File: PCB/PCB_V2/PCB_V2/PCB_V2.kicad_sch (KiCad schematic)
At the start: 99 parts, among them J1 GND, J2 VIN, J3 GND, J4 VIN, J5 VOUT, J6 GND, J7 VOUT, J8 GND, Q1 BC817-40(SOT23), Q2 BC817-40(SOT23), T1 LMUN2211LT1G(SOT-23), U1 ESP32-WROOM-32E-N4, U2 CH340X(MSOP-10), U3 LAN8710A-EZC(QFN32)

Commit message: Changes Part 1 for the PCB Files
Most recent update for the PCB Design
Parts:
- removed C23, C24, C25, C26: C, symbol Device:C
- removed D5, D6: D, symbol Device:D
- removed J1, J3, J6, J8: GND, symbol Connector:Conn_01x01_Pin
- removed J2, J4: VIN, symbol Connector:Conn_01x01_Pin
- removed J5, J7: VOUT, symbol Connector:Conn_01x01_Pin
- removed L3, L4: L, symbol Device:L
- removed R24, R25, R26, R27, R28, R29, R30, R31: R_US, symbol Device:R_US
- removed R34: 52.3k, symbol Jumper:SolderJumper_2_Open
- removed R35, R37: 10k, symbol Device:R_US
- removed R36: 140k, symbol Jumper:SolderJumper_2_Open
- removed U4, U5: ~, symbol buck converter module:mp1584
- added D10, D8, D9: 1N4007, Diode_THT:D_DO-41_SOD81_P10.16mm_Horizontal, symbol Diode:1N4007
- added D11: 1N5822, Diode_THT:D_DO-201AD_P15.24mm_Horizontal, symbol Diode:1N5822
- added D5, D6, D7: LED, LED_THT:LED_D3.0mm, symbol Device:LED
- added J11, J12, J13: Screw_Terminal_01x03, TerminalBlock_Phoenix:TerminalBlock_Phoenix_MKDS-1,5-3-5.08_1x03_P5.08mm_Horizontal, symbol Connector:Screw_Terminal_01x03
- added J14: PSU_I/P, TerminalBlock_Phoenix:TerminalBlock_Phoenix_MKDS-1,5-3-5.08_1x03_P5.08mm_Horizontal, symbol Connector:Screw_Terminal_01x02
- added J15: Battery_I/P, TerminalBlock_Phoenix:TerminalBlock_Phoenix_MKDS-1,5-3-5.08_1x03_P5.08mm_Horizontal, symbol Connector:Screw_Terminal_01x02
- added J19: LEDs Ground, symbol Connector:Screw_Terminal_01x03
- added K1, K2, K3: FINDER-34.51.7xxx.x019, Relay_THT:Relay_SPDT_Finder_34.51_Horizontal, symbol Relay:FINDER-34.51.7xxx.x019
- added Q3, Q4, Q5: BC546, Package_TO_SOT_THT:TO-92_Inline, symbol Transistor_BJT:BC546
- added R24, R26: 140k, Resistor_SMD:R_0603_1608Metric_Pad0.98x0.95mm_HandSolder, symbol Device:R
- added R25, R27, R29: 10k, Resistor_SMD:R_0603_1608Metric_Pad0.98x0.95mm_HandSolder, symbol Device:R
- added R28: 52.3k, Resistor_SMD:R_0603_1608Metric_Pad0.98x0.95mm_HandSolder, symbol Device:R
- added R30, R38, R40: 2.2k, Resistor_SMD:R_0805_2012Metric, symbol Device:R
- added R31, R39, R41: 3.3k, Resistor_SMD:R_0805_2012Metric, symbol Device:R
- added R32, R33, R34: 300, Resistor_SMD:R_0603_1608Metric, symbol Device:R
- added R35, R36, R37: 1k, Resistor_SMD:R_0603_1608Metric, symbol Device:R
- added R42, R44: 10k, symbol Device:R
- added R43, R45: 2.2k, symbol Device:R
- added U4: AMS1117-3.3, Package_TO_SOT_SMD:SOT-223-3_TabPin2, symbol Regulator_Linear:AMS1117-3.3
- added U5, U6, U7: ACS712xLCTR-20A, Package_SO:SOIC-8_3.9x4.9mm_P1.27mm, symbol Sensor_Current:ACS712xLCTR-20A
- C15: value C -> 10uF; footprint (none) -> Capacitor_SMD:C_0805_2012Metric
- C16, C19, C21: value C -> 100nF; footprint (none) -> Capacitor_SMD:C_0805_2012Metric
- C17, C20, C22: value C -> 1nF; footprint (none) -> Capacitor_SMD:C_0805_2012Metric
- C18: value C -> 22uF; footprint (none) -> Capacitor_SMD:C_0805_2012Metric
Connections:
- net GND: now also C15.2, C16.2, C17.2, C18.2, C19.2, C20.2, C21.2, C22.2, J14.2 (Pin_2), J15.2 (Pin_2), J19.1 (Pin_1), J19.2 (Pin_2), J19.3 (Pin_3), Q3.3 (E), Q4.3 (E), Q5.3 (E), R25.2, R27.2, R29.2, R31.2, R39.2, R41.2, R43.2, R45.2, U4.1 (GND), U5.5 (GND), U6.5 (GND), U7.5 (GND)
- net BC1_5_O/P: now reaches C19.1
- net BC1_5_O/P: now also C15.1, C16.1, C21.1, D10.1 (K), D8.1 (K), D9.1 (K), K1.A1, K2.A1, K3.A1, R28.1, R32.1, R33.1, R34.1, U4.3 (VI), U5.8 (VCC), U6.8 (VCC), U7.8 (VCC)
- net AMS1117_O/P: now reaches C18.1
- net AMS1117_O/P: now also U4.2 (VO); no longer C16.1
- net at C20.1: now also U6.6 (FILTER)
- net at C17.1: now also U5.6 (FILTER); no longer C15.1
- net at C22.1: now also U7.6 (FILTER)
- new net: R42.2, R43.1
- new net: R38.1, U6.7 (VIOUT)
- new net: D6.1 (K), D9.2 (A), K2.A2, Q4.1 (C)
- new net: Q4.2 (B), R36.1
- new net: U5.1 (IP+), U5.2 (IP+)
- new net: U5.3 (IP-), U5.4 (IP-)
- new net: R30.1, U5.7 (VIOUT)
- new net: D10.2 (A), D7.1 (K), K3.A2, Q5.1 (C)
- new net: D7.2 (A), R34.2
- new net: Q3.2 (B), R35.1
- new net: D5.1 (K), D8.2 (A), K1.A2, Q3.1 (C)
- new net: R28.2, R29.1
- new net: Q5.2 (B), R37.1
- new net: R40.1, U7.7 (VIOUT)
- new net: D5.2 (A), R32.2
- new net: R44.2, R45.1
- new net: D6.2 (A), R33.2
- new net +14.5V: D11.2 (A), J14.1 (Pin_1), R42.1
- new net BC2_12_O/P_1: R24.1
- new net BC3_12_O/P_2: R26.1, U6.1 (IP+), U6.2 (IP+), U7.1 (IP+), U7.2 (IP+)
- new net COM1: J11.2 (Pin_2), K1.11
- new net COM2: J12.2 (Pin_2), K2.11, U6.3 (IP-), U6.4 (IP-)
- new net COM3: J13.2 (Pin_2), K3.11, U7.3 (IP-), U7.4 (IP-)
- new net CURRENT_SENSE_1: R30.2, R31.1
- new net CURRENT_SENSE_2: R38.2, R39.1
- new net CURRENT_SENSE_3: R40.2, R41.1
- new net MAIN_OP: D11.1 (K), J15.1 (Pin_1), R44.1
- new net MP1584ENCircuit1/Feedback: R24.2, R25.1
- new net MP1584ENCircuit2/Feedback: R26.2, R27.1
- new net NC1: J11.1 (Pin_1), K1.12
- new net NC2: J12.1 (Pin_1), K2.12
- new net NC3: J13.1 (Pin_1), K3.12
- new net NO1: J11.3 (Pin_3), K1.14
- new net NO2: J12.3 (Pin_3), K2.14
- new net NO3: J13.3 (Pin_3), K3.14
- new net RELAY_1_CTRL: R35.2
- new net RELAY_2_CTRL: R36.2
- new net RELAY_3_CTRL: R37.2
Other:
- added sheet MP1584ENCircuit (MP1584ENCircuit.kicad_sch)
- added sheet MP1584ENCircuit1 (MP1584ENCircuit.kicad_sch)
- added sheet MP1584ENCircuit2 (MP1584ENCircuit.kicad_sch)
- note removed: "For fixed output voltage value, remove potentiometer R1 and install resistor at open pads R11. They work together with R2 to form voltage divider feedback for MP1584."
- note removed: "R4 controls oscillating frequency"
- note removed: "R5+R6 = voltage divider. MP1584 starts at > 1.5V. MP1584 sleeps at < 1.2V."

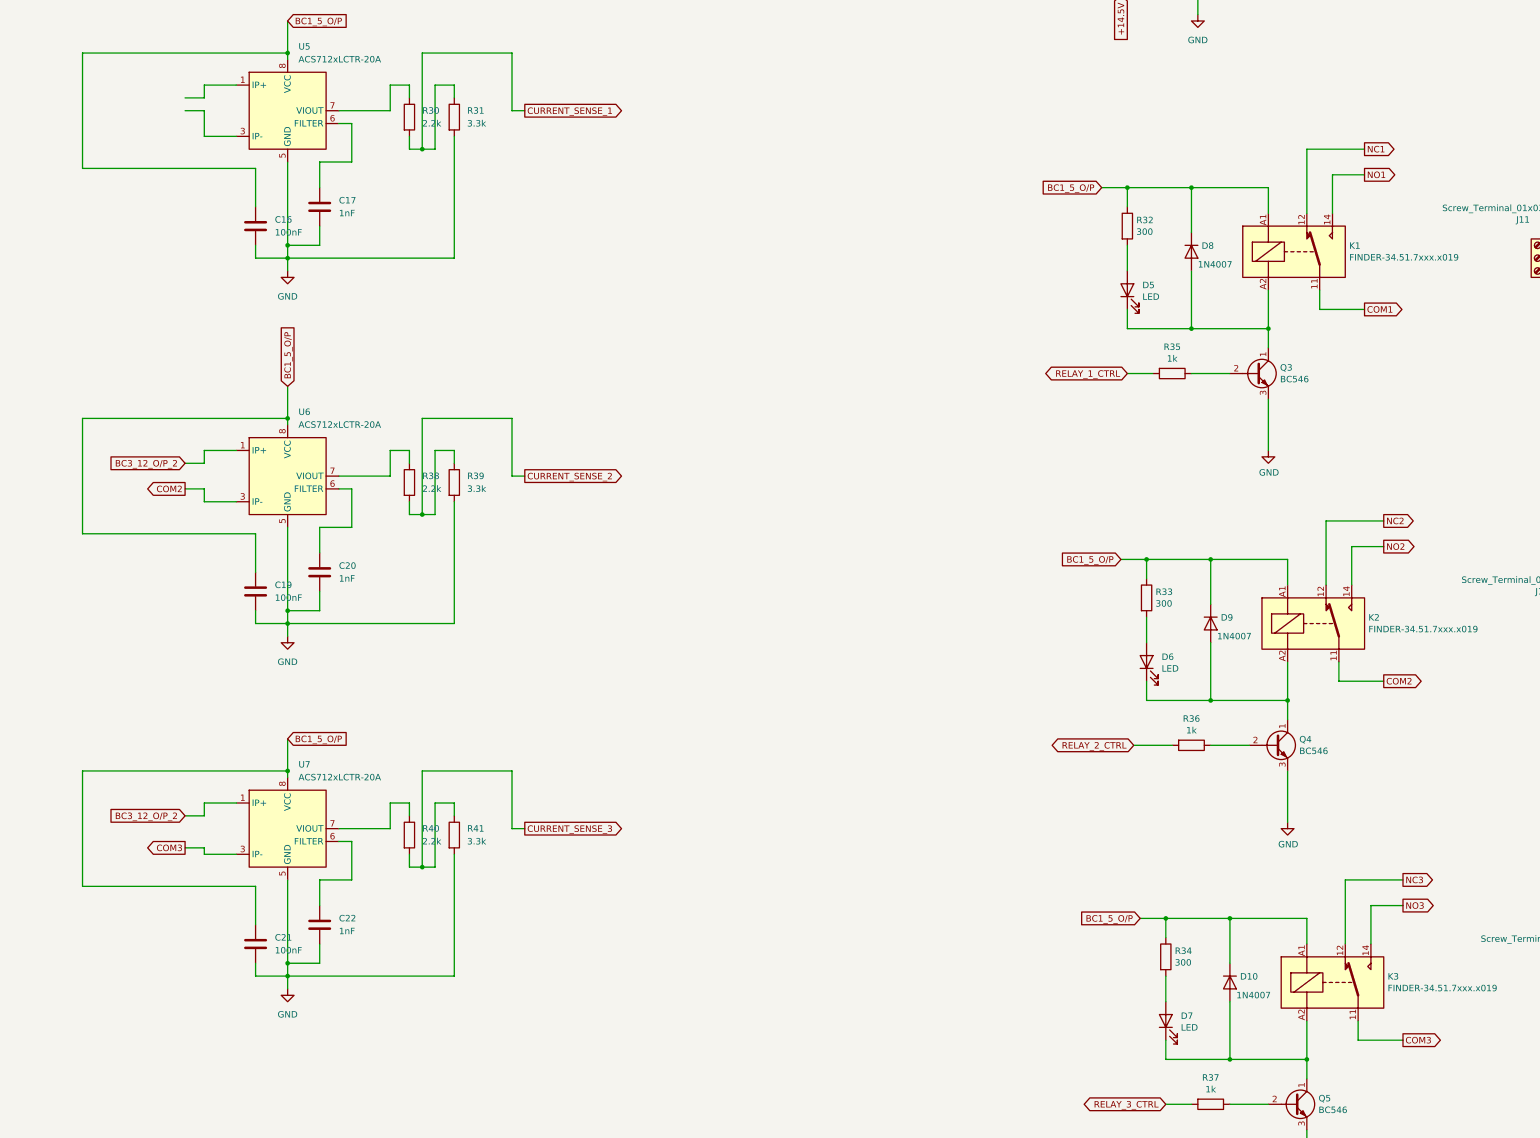
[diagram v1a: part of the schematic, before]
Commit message: Updatign the files of the PCB folder
- seld design modules completed, with the correct math
- schematic for pcb v2 completed
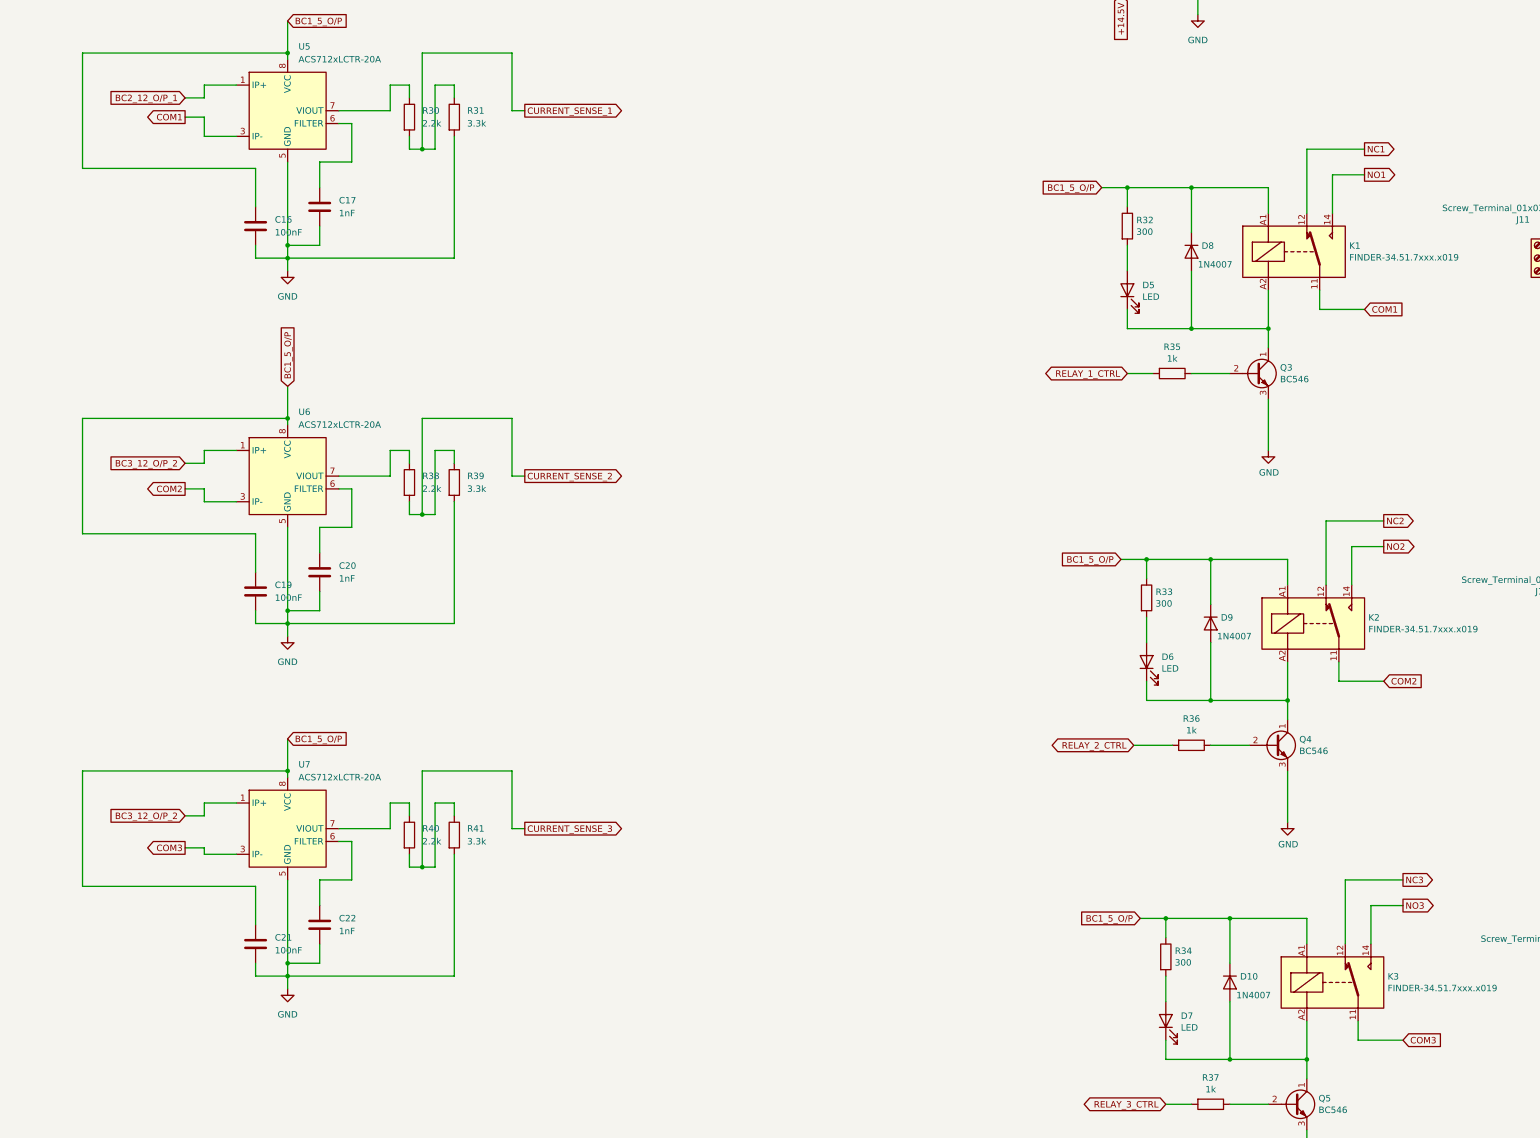
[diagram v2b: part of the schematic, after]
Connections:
- net BC2_12_O/P_1: now also U5.1 (IP+), U5.2 (IP+)
- net COM1: now also U5.3 (IP-), U5.4 (IP-)
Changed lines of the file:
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@@
 	(wire
 		(pts
-			(xy 341.63 234.95) (xy 341.63 240.03)
+			(xy 341.63 236.22) (xy 341.63 240.03)
 		)
 		(stroke
@@
 	(wire
 		(pts
-			(xy 337.82 234.95) (xy 341.63 234.95)
+			(xy 337.82 236.22) (xy 341.63 236.22)
 		)
 		(stroke
@@
 	)
 	(global_label "COM1"
-		(shape output)
+		(shape input)
 		(at 571.5 274.32 0)
 		(effects
@@
 		)
 	)
+	(global_label "COM1"
+		(shape output)
+		(at 337.82 236.22 180)
+		(fields_autoplaced yes)
+		(effects
+			(font
+				(size 1.27 1.27)
+			)
+			(justify right)
+		)
+		(property "Intersheetrefs" "${INTERSHEET_REFS}"
+			(at 329.5734 236.22 0)
+			(hide yes)
+			(show_name no)
+			(do_not_autoplace no)
+			(effects
+				(font
+					(size 1.27 1.27)
+				)
+				(justify right)
+			)
+		)
+	)
 	(global_label "NC3"
 		(shape output)
@@
 	)
 	(global_label "COM3"
-		(shape output)
+		(shape input)
 		(at 579.12 419.1 0)
 		(effects
@@
 		)
 	)
+	(global_label "BC2_12_O{slash}P_1"
+		(shape input)
+		(at 337.82 232.41 180)
+		(fields_autoplaced yes)
+		(effects
+			(font
+				(size 1.27 1.27)
+			)
+			(justify right)
+		)
+		(property "Intersheetrefs" "${INTERSHEET_REFS}"
+			(at 320.623 232.41 0)
+			(hide yes)
+			(show_name no)
+			(do_not_autoplace no)
+			(effects
+				(font
+					(size 1.27 1.27)
+				)
+				(justify right)
+			)
+		)
+	)
 	(global_label "CURRENT_SENSE_1"
 		(shape output)
@@
 	)
 	(global_label "COM2"
-		(shape output)
+		(shape input)
 		(at 575.31 347.98 0)
 		(effects

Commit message: Pushing most recent changes - 10/6/2026
1. Finished the schematics of all the individual modules
2. Made the changes to errors and the hierarchal issues for the MP1584
3. Fixed the open connections for the OLIMEX ESP32 and the labeling for the same

TO DO//
1. Check the current warnings while running ERC (single label warnings and the no connect ones)
2. The tracing and component placement needs to be finalised
3. EMI/EMC placement for the modules needs to be kept in mind with a priority
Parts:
- added D12, D13, D14, D15: LED, LED_SMD:LED_0805_2012Metric, symbol Device:LED
- added R46, R47, R48, R49: 1k, Resistor_SMD:R_0805_2012Metric, symbol Device:R
- D10: renamed from D9; value 1N4007 -> M7; footprint Diode_THT:D_DO-41_SOD81_P10.16mm_Horizontal -> Diode_SMD:D_SMA
- D11: renamed from D10; value 1N4007 -> M7; footprint Diode_THT:D_DO-41_SOD81_P10.16mm_Horizontal -> Diode_SMD:D_SMA
- D5: renamed from D11; value 1N5822 -> SS54; footprint Diode_THT:D_DO-201AD_P15.24mm_Horizontal -> Diode_SMD:D_SMC
- D6: renamed from D5; footprint LED_THT:LED_D3.0mm -> LED_SMD:LED_0805_2012Metric
- D7: renamed from D6; footprint LED_THT:LED_D3.0mm -> LED_SMD:LED_0805_2012Metric
- D8: renamed from D7; footprint LED_THT:LED_D3.0mm -> LED_SMD:LED_0805_2012Metric
- D9: renamed from D8; value 1N4007 -> M7; footprint Diode_THT:D_DO-41_SOD81_P10.16mm_Horizontal -> Diode_SMD:D_SMA
- J1: renamed from J14; footprint TerminalBlock_Phoenix:TerminalBlock_Phoenix_MKDS-1,5-3-5.08_1x03_P5.08mm_Horizontal -> TerminalBlock_Phoenix:TerminalBlock_Phoenix_MKDS-1,5-2-5.08_1x02_P5.08mm_Horizontal
- J2: renamed from J15; footprint TerminalBlock_Phoenix:TerminalBlock_Phoenix_MKDS-1,5-3-5.08_1x03_P5.08mm_Horizontal -> TerminalBlock_Phoenix:TerminalBlock_Phoenix_MKDS-1,5-2-5.08_1x02_P5.08mm_Horizontal
- J3: renamed from J19; footprint (none) -> TerminalBlock_Phoenix:TerminalBlock_Phoenix_MKDS-1,5-3_1x03_P5.00mm_Horizontal
- J4: renamed from J11; value Screw_Terminal_01x03 -> Relay_1_Terminal
- J5: renamed from J12; value Screw_Terminal_01x03 -> Relay_2_Terminal
- J6: renamed from J13; value Screw_Terminal_01x03 -> Relay_3_Terminal
- Q3, Q4, Q5: value BC546 -> BC846; footprint Package_TO_SOT_THT:TO-92_Inline -> Package_TO_SOT_SMD:SOT-23
- R30: renamed from R42; footprint (none) -> Resistor_SMD:R_0805_2012Metric
- R31: renamed from R43; footprint (none) -> Resistor_SMD:R_0805_2012Metric
- R32: renamed from R44; footprint (none) -> Resistor_SMD:R_0805_2012Metric
- R33: renamed from R45; footprint (none) -> Resistor_SMD:R_0805_2012Metric
- R40: renamed from R24; footprint Resistor_SMD:R_0603_1608Metric_Pad0.98x0.95mm_HandSolder -> Resistor_SMD:R_0603_1608Metric
- R41: renamed from R25; footprint Resistor_SMD:R_0603_1608Metric_Pad0.98x0.95mm_HandSolder -> Resistor_SMD:R_0603_1608Metric
- R42: renamed from R26; footprint Resistor_SMD:R_0603_1608Metric_Pad0.98x0.95mm_HandSolder -> Resistor_SMD:R_0603_1608Metric
- R43: renamed from R27; footprint Resistor_SMD:R_0603_1608Metric_Pad0.98x0.95mm_HandSolder -> Resistor_SMD:R_0603_1608Metric
- R44: renamed from R28; footprint Resistor_SMD:R_0603_1608Metric_Pad0.98x0.95mm_HandSolder -> Resistor_SMD:R_0603_1608Metric
- R45: renamed from R29; footprint Resistor_SMD:R_0603_1608Metric_Pad0.98x0.95mm_HandSolder -> Resistor_SMD:R_0603_1608Metric
- renumbered C19 to C17, C21 to C18, C17 to C19, C22 to C21, C18 to C22, R30 to R24, R38 to R25, R40 to R26, R31 to R27, R39 to R28, R41 to R29, R32 to R34, R33 to R35, R34 to R36, R35 to R37, R36 to R38, R37 to R39
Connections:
- net GPI35 is gone; now on net CURRENT_SENSE_2: U1.7 (GPI35/ADC1_CH7/RTC_GPIO5)
- net GPI36\U1RXD is gone; now on net PSU_ESP: U1.4 (GPI36/SENSOR_VP/ADC1_CH0/RTC_GPIO0)
- net GPI39 is gone; now on net BATT_VD: U1.5 (GPI39/SENSOR_VN/ADC1_CH3/RTC_GPIO3)
- net GPIO13\I2C-SDA is gone; now on net RELAY_2_CTRL: U1.16 (GPIO13/ADC2_CH4/TOUCH4/RTC_GPIO14/MTCK/HSPID/HS2_DATA3/SD_DATA3/EMAC_RX_ER)
- net GPIO32 is gone; now on net CURRENT_SENSE_3: U1.8 (GPIO32/XTAL_32K_P/ADC1_CH4/TOUCH9/RTC_GPIO9)
- net GPIO33 is gone; now on net CURRENT_SENSE_1: U1.9 (GPIO33/XTAL_32K_N/ADC1_CH5/TOUCH8/RTC_GPIO8)
- net GPIO4\U1TXD is gone; now on net RELAY_1_CTRL: U1.26 (GPIO4/ADC2_CH0/TOUCH0/RTC_GPIO10/HSPIHD/HS2_DATA1/SD_DATA1/EMAC_TX_ER)
- net +3.3V: no longer U1.2 (VDD33(3V3))
- net AMS1117_O/P: now also U1.2 (VDD33(3V3)), R46.2
- net BC1_5_O/P: now also R47.2
- net BC2_12_O/P_1: now also R48.2
- net BC3_12_O/P_2: now also R49.2
- net GND: now also D12.1 (K), D13.1 (K), D14.1 (K), D15.1 (K)
- net GPIO12\PHY_PWR: no longer U1.14 (GPIO12/ADC2_CH5/TOUCH5/RTC_GPIO15/MTDI/HSPIQ/HS2_DATA2/SD_DATA2/EMAC_TXD3)
- net RELAY_3_CTRL: now also U1.14 (GPIO12/ADC2_CH5/TOUCH5/RTC_GPIO15/MTDI/HSPIQ/HS2_DATA2/SD_DATA2/EMAC_TXD3)
- net PSU_ESP: now reaches R30.2, R31.1
- net MP1584ENCircuit/Feedback: now reaches R44.2, R45.1
- net BATT_VD: now reaches R32.2, R33.1
- new net: D15.2 (A), R49.1
- new net: D14.2 (A), R48.1
- new net: D12.2 (A), R46.1
- new net: D13.2 (A), R47.1
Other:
- sheet MP1584ENCircuit ports: added Feedback, GND; removed gnd
- sheet MP1584ENCircuit1 ports: added GND; removed gnd
- sheet MP1584ENCircuit2 ports: added GND; removed gnd
- note added: "Buck Converters"
- note added: "Current sensors"
- note added: "Diagnostic LEDs"
- note added: "Power and Voltage Dividers"
- note added: "Relays"
- note added: "Voltage Regulator 3.3V"
- note removed: "!!!WARNING!!! When the board is powered via PoE, don't include the USB cable for to programming it!!! In case this is required, USB-ISO must be used for to guarantee galvanic isolation! See: https://www.olimex.com/Products/USB-Modules/USB-ISO/"
- moved on the sheet: BUT1, D10, D11, D5, D6, D7, D8, D9, J1, J2, J3, J4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
